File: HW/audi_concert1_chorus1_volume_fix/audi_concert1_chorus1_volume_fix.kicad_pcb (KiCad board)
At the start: 2 copper layers, 32.8 x 26.2 mm, 39 parts, among them CON1 I2C_to_TDA, CON2 USB, CON3 SPI_TO_PANEL, CON4 JLINK, U1 68HC05_PLCC, U2 AP1117-33, U3 STM32F103C8Tx, U4 MAX809, Y1 32.768kHz, Y2 8MHz

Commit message: v2.0
Signed-off-by: Tomas kovacik <nail@nodomain.sk>
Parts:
- added R1: 1k, Resistors_SMD.pretty:R_0805_HandSoldering, F.Cu at (114.0, 90.4)
- moved JP1 68.6 mm to (113.1, 74.0)
- moved R8 68.3 mm to (117.8, 74.0)
- moved R14 67.0 mm to (127.9, 85.1)
- moved CON3 66.4 mm to (132.2, 90.4)
- moved R16 66.3 mm to (127.8, 93.6)
- moved C8 66.2 mm to (103.4, 92.7)
- moved CON1 66.2 mm to (103.4, 72.9)
- moved Y1 66.2 mm to (108.5, 74.4)
- moved C2 66.2 mm to (110.8, 74.0)
- moved C4 66.2 mm to (108.1, 77.9)
- moved C5 66.2 mm to (108.1, 85.9)
- moved C6 66.2 mm to (108.1, 88.1)
- moved JP2 66.2 mm to (116.6, 93.6)
- moved R11 66.2 mm to (127.9, 78.9)
- moved R13 66.2 mm to (127.9, 89.3)
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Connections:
- U1 pad 23: (no net) -> /GALA
- U3 pad 10: (no net) -> Net-(R1-Pad2)
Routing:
- net /GALA: track 0.00 -> 16.7 mm, vias 0 -> 1
- net Net-(R1-Pad2): track 0.00 -> 7.28 mm
- net Net-(CON2-Pad3): track 55.3 -> 49.5 mm
- net /TX: track 19.3 -> 23.5 mm
- net /SCL_FROM_MOTO: track 19.6 -> 15.6 mm
- net 5V: track 48.3 -> 52.3 mm
- net /BOOT0: track 8.40 -> 5.28 mm
- net GND: track 109.8 -> 106.9 mm, vias 14 -> 16
- net /SDA_TO_TDA: track 26.1 -> 23.4 mm
- net /RESET: track 20.7 -> 23.2 mm
- net 3V3: track 101.0 -> 103.2 mm
- net /SCL_TO_TDA: track 27.6 -> 25.4 mm
- net /DATA_FROM_MCU: track 7.37 -> 5.27 mm
- net /RX: track 25.5 -> 23.5 mm
- net /RESET_KA: track 29.2 -> 27.5 mm
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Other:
- board text added: "5V|D-|D+|GND"
- board text added: "CL|DA|ST"
- board text added: "TX|RX|3v|IO|CL|GD"

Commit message: HW v3
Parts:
- added R21: 10k, Resistors_SMD.pretty:R_0805_HandSoldering, F.Cu at (120.6, 74.0)
- added R22: 10k, Resistors_SMD.pretty:R_0805_HandSoldering, F.Cu at (128.0, 91.5)
- moved R17 4.09 mm to (128.0, 95.6)
- moved R15 3.84 mm to (124.2, 94.4), turned to 90 degrees
- moved D1 1.69 mm to (121.9, 94.2)
- moved R2 1.65 mm to (119.6, 93.2)
- moved R3 1.53 mm to (117.6, 93.2)
- moved R20 1.34 mm to (118.6, 74.0)
- moved JP2 1.31 mm to (115.3, 93.9)
- moved R8 1.22 mm to (116.6, 74.0)
- moved C7 1.14 mm to (114.6, 74.1)
- moved U4 0.76 mm to (112.4, 94.3)
- moved JP1 0.74 mm to (112.4, 74.1)
- moved C2 0.47 mm to (110.3, 74.1)
- moved R19 0.46 mm to (122.6, 74.0)
- moved C3 0.42 mm to (105.9, 74.4)
- moved R7 0.38 mm to (124.6, 74.0)
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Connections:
- CON3 pad 1: /STATUS_TO_PANEL -> /DATA_TO_PANEL
- CON3 pad 2: /DATA_TO_PANEL -> /STATUS_TO_PANEL
- U3 pad 25: (no net) -> Net-(R17-Pad2)
- U3 pad 28: Net-(R17-Pad2) -> Net-(R22-Pad2)
- U3 pad 41: Net-(R19-Pad2) -> Net-(R21-Pad2)
- U3 pad 45: (no net) -> Net-(R19-Pad2)
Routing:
- net GND: track 106.9 -> 87.2 mm
- net /DATA_FROM_MCU: track 5.27 -> 18.1 mm, vias 1 -> 2
- net 3V3: track 103.2 -> 115.7 mm, vias 3 -> 4
- net Net-(R21-Pad2): track 0.00 -> 11.6 mm, vias 0 -> 2
- net Net-(R22-Pad2): track 0.00 -> 9.41 mm
- net /CLOCK_TO_PANEL: track 3.41 -> 9.01 mm
- net /RESET_KA: track 27.5 -> 32.4 mm
- net Net-(R15-Pad2): track 13.0 -> 8.39 mm
- net /SWDCLK: track 13.7 -> 18.1 mm
- net /TX: track 23.5 -> 19.5 mm
- net Net-(R17-Pad2): track 9.48 -> 12.6 mm
- net Net-(R4-Pad1): track 8.82 -> 11.3 mm
- net Net-(R5-Pad2): track 10.1 -> 12.3 mm
- net Net-(R6-Pad1): track 11.6 -> 13.9 mm
- net /DATA_TO_PANEL: track 3.60 -> 5.59 mm
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
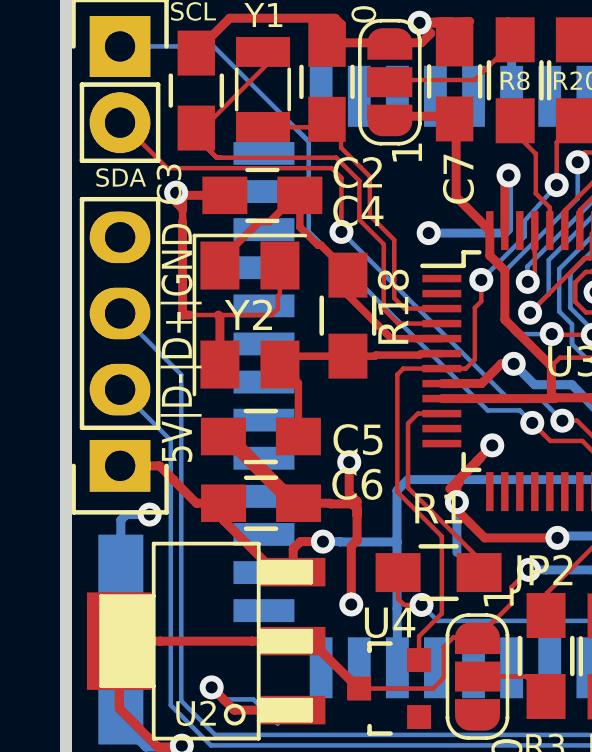
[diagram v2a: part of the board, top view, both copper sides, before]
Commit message: silk screen positioning
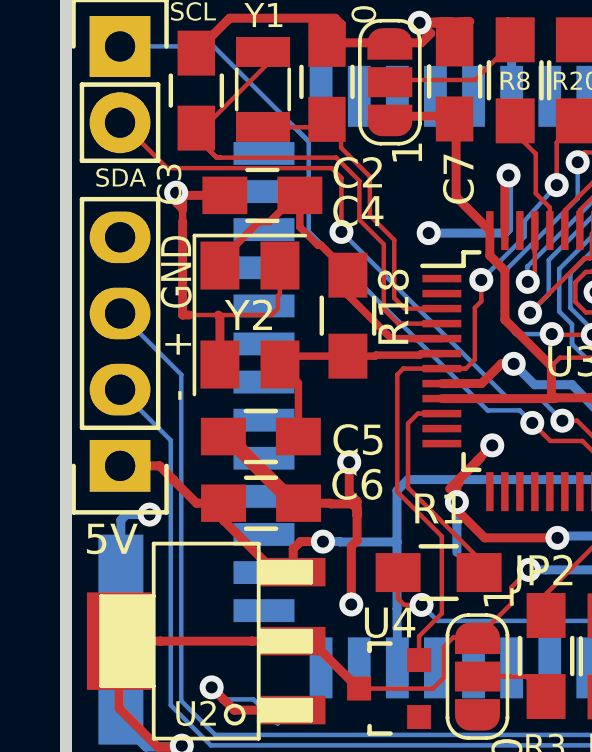
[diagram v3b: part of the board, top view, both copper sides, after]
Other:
- board text added: "- + GND"
- board text added: "5V"

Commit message: HW3
Signed-off-by: Tomas kovacik <nail@nodomain.sk>
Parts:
- added Q1: BSS138, TO_SOT_Packages_SMD:SOT-23, F.Cu at (127.4, 94.3)
- added Q2: BSS138, TO_SOT_Packages_SMD:SOT-23, F.Cu at (127.4, 79.9)
- added R23: 10k, Resistors_SMD.pretty:R_0805_HandSoldering, F.Cu at (131.6, 85.9)
- added R24: 10k, Resistors_SMD.pretty:R_0805_HandSoldering, B.Cu at (131.6, 85.9)
- R17, R5: moved to B.Cu
- R7: footprint Resistors_SMD.pretty:R_0805_HandSoldering -> Resistors_SMD.pretty:R_0603_HandSoldering
- moved R5 3.96 mm to (131.5, 79.5), turned to 90 degrees
- moved R17 3.88 mm to (131.6, 94.1), turned to -90 degrees
- moved R11 3.72 mm to (131.5, 79.5), turned to 90 degrees
- moved R16 3.65 mm to (131.6, 94.1), turned to -90 degrees
- moved CON4 2.07 mm to (134.0, 74.2)
- moved CON3 1.90 mm to (134.1, 90.2)
- moved D1 1.07 mm to (122.0, 93.2)
- moved R15 0.76 mm to (124.3, 93.6)
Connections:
- R11 pad 1: Net-(R11-Pad1) -> Net-(Q2-Pad1)
- R17 pad 2: Net-(R17-Pad2) -> Net-(Q1-Pad1)
- U3 pad 14: (no net) -> Net-(Q2-Pad3)
- U3 pad 25: Net-(R17-Pad2) -> Net-(Q1-Pad3)
- U3 pad 38: Net-(R11-Pad1) -> (no net)
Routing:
- net Net-(Q2-Pad3): track 0.00 -> 24.8 mm, vias 0 -> 1
- net Net-(Q1-Pad3): track 0.00 -> 23.6 mm, vias 0 -> 2
- net Net-(R17-Pad2): track 12.6 -> 0.00 mm
- net 3V3: track 115.7 -> 126.4 mm, vias 4 -> 3
- net Net-(R11-Pad1): track 9.81 -> 0.00 mm
- net Net-(R16-Pad2): track 10.4 -> 16.8 mm
- net Net-(Q1-Pad1): track 0.00 -> 5.98 mm, vias 0 -> 1
- net Net-(CON2-Pad2): track 46.9 -> 42.6 mm
- net Net-(CON2-Pad3): track 49.3 -> 45.4 mm
- net Net-(R5-Pad2): track 12.3 -> 16.1 mm, vias 0 -> 1
- net Net-(Q2-Pad1): track 0.00 -> 3.72 mm
- net /CLOCK_TO_PANEL: track 9.01 -> 11.2 mm
- net /SCL_FROM_MOTO: track 15.6 -> 17.7 mm
- net /SWDCLK: track 18.1 -> 20.1 mm
- net /STATUS_TO_PANEL: track 4.04 -> 2.32 mm
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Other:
- board size 32.8 x 26.2 mm -> 34 x 26.2 mm
- board text added: "CLK DATA"
- board text added: "STA TUS"
- board text removed: "CLK DATA STATUS"
